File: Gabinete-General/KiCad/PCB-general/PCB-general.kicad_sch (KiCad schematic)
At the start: 6 parts, among them J2 TFT Display, U1 ESP32-S3-DevKitC, U2 LM7805_TO220

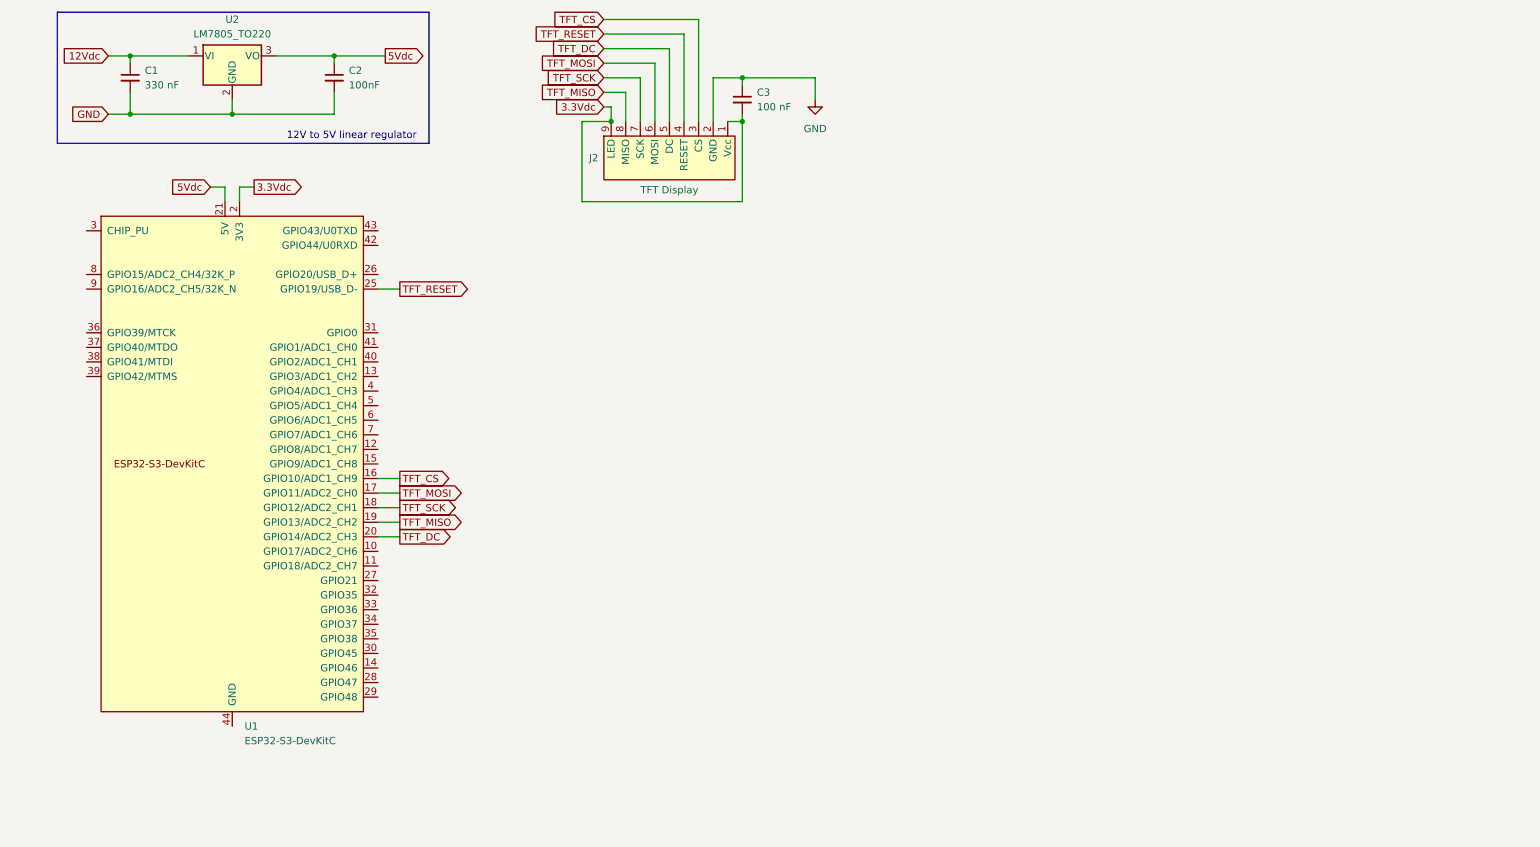
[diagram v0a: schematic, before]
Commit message: Finalizar esquemático PCB control general
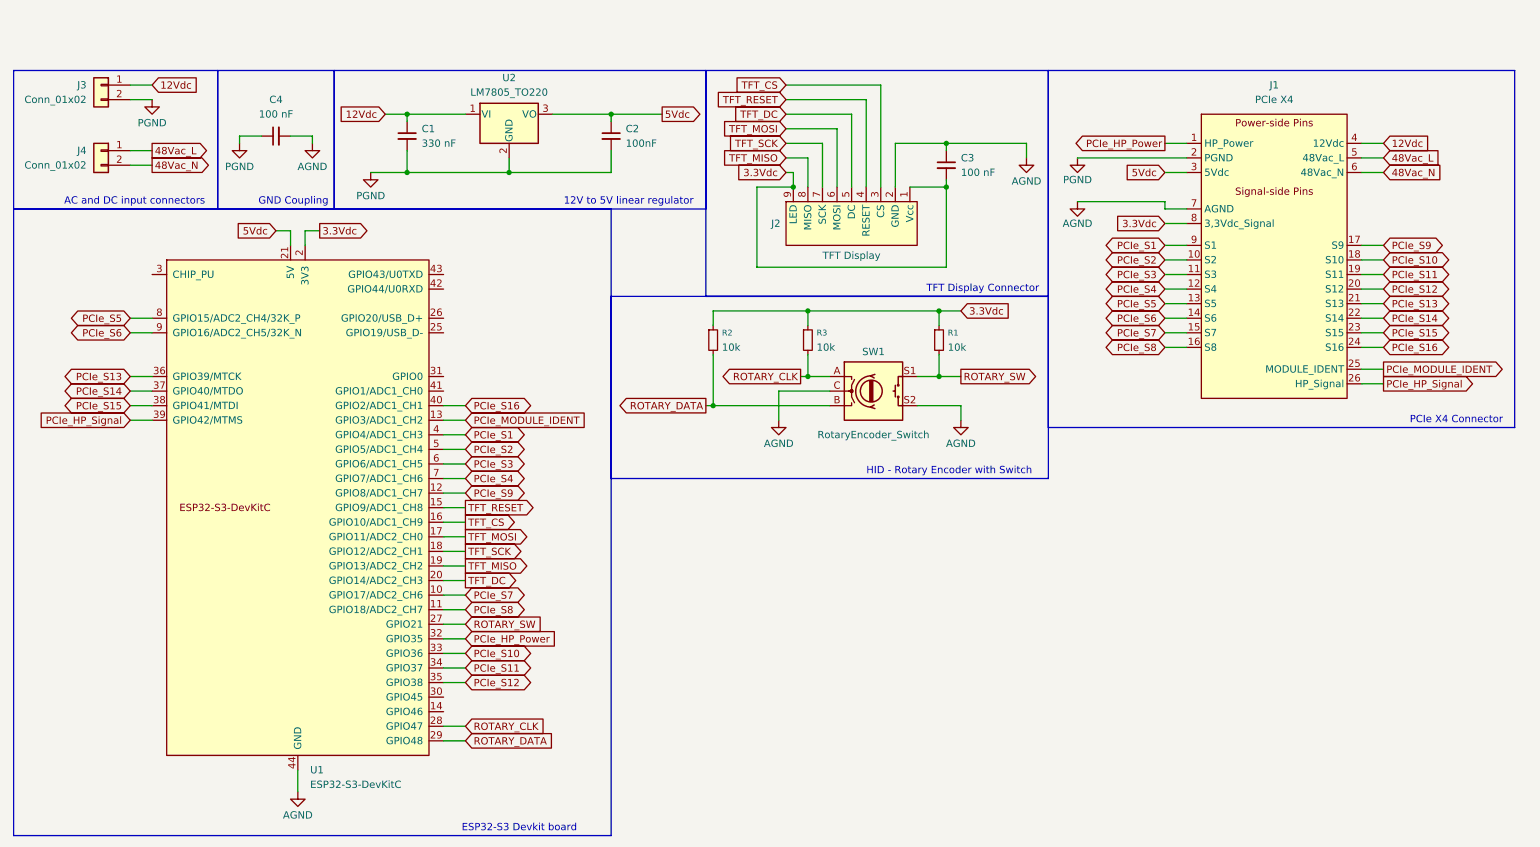
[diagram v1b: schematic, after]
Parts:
- added C4: 100 nF, symbol Device:C_Small
- added J1: PCIe X4, symbol Proyecto_Final:PCIE_x4_NSH_pcb_general
- added J3, J4: Conn_01x02, symbol Connector_Generic:Conn_01x02
- added R1, R2, R3: 10k, symbol Device:R_Small
- added SW1: RotaryEncoder_Switch, symbol Device:RotaryEncoder_Switch
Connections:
- net 12Vdc: now also J1.4 (12Vdc), J3.1 (Pin_1)
- net 3.3Vdc: now also J1.8 (3,3Vdc_Signal), R1.1, R2.1, R3.1
- net 5Vdc: now also J1.3 (5Vdc)
- net TFT_RESET: now also U1.15 (GPIO9/ADC1_CH8); no longer U1.25 (GPIO19/USB_D-)
- net PCIe_S7: now reaches U1.10 (GPIO17/ADC2_CH6)
- net PCIe_S7: now also J1.15 (S7)
- net PCIe_S8: now reaches U1.11 (GPIO18/ADC2_CH7)
- net PCIe_S8: now also J1.16 (S8)
- net PCIe_S9: now reaches U1.12 (GPIO8/ADC1_CH7)
- net PCIe_S9: now also J1.17 (S9)
- net PCIe_MODULE_IDENT: now reaches U1.13 (GPIO3/ADC1_CH2)
- net PCIe_MODULE_IDENT: now also J1.25 (MODULE_IDENT)
- net AGND: now reaches U1.22 (GND), U1.23 (GND), U1.24 (GND), U1.44 (GND)
- net AGND: now also C3.1, J2.2 (GND), C4.2, J1.7 (AGND), SW1.C, SW1.S2
- net ROTARY_SW: now reaches U1.27 (GPIO21)
- net ROTARY_SW: now also R1.2, SW1.S1
- net ROTARY_CLK: now reaches U1.28 (GPIO47)
- net ROTARY_CLK: now also R3.2, SW1.A
- net ROTARY_DATA: now reaches U1.29 (GPIO48)
- net ROTARY_DATA: now also R2.2, SW1.B
- net PCIe_HP_Power: now reaches U1.32 (GPIO35)
- net PCIe_HP_Power: now also J1.1 (HP_Power)
- net PCIe_S10: now reaches U1.33 (GPIO36)
- net PCIe_S10: now also J1.18 (S10)
- net PCIe_S11: now reaches U1.34 (GPIO37)
- net PCIe_S11: now also J1.19 (S11)
- net PCIe_S12: now reaches U1.35 (GPIO38)
- net PCIe_S12: now also J1.20 (S12)
- net PCIe_S13: now reaches U1.36 (GPIO39/MTCK)
- net PCIe_S13: now also J1.21 (S13)
- net PCIe_S14: now reaches U1.37 (GPIO40/MTDO)
- net PCIe_S14: now also J1.22 (S14)
- net PCIe_S15: now reaches U1.38 (GPIO41/MTDI)
- net PCIe_S15: now also J1.23 (S15)
- net PCIe_HP_Signal: now reaches U1.39 (GPIO42/MTMS)
- net PCIe_HP_Signal: now also J1.26 (HP_Signal)
- net PCIe_S1: now reaches U1.4 (GPIO4/ADC1_CH3)
- net PCIe_S1: now also J1.9 (S1)
- net PCIe_S16: now reaches U1.40 (GPIO2/ADC1_CH1)
- net PCIe_S16: now also J1.24 (S16)
- net PCIe_S2: now reaches U1.5 (GPIO5/ADC1_CH4)
- net PCIe_S2: now also J1.10 (S2)
- net PCIe_S3: now reaches U1.6 (GPIO6/ADC1_CH5)
- net PCIe_S3: now also J1.11 (S3)
- net PCIe_S4: now reaches U1.7 (GPIO7/ADC1_CH6)
- net PCIe_S4: now also J1.12 (S4)
- net PCIe_S5: now reaches U1.8 (GPIO15/ADC2_CH4/32K_P)
- net PCIe_S5: now also J1.13 (S5)
- net PCIe_S6: now reaches U1.9 (GPIO16/ADC2_CH5/32K_N)
- net PCIe_S6: now also J1.14 (S6)
- net GND renamed PGND
- net PGND: now also C4.1, J1.2 (PGND), J3.2 (Pin_2); no longer C3.1, J2.2 (GND)
- new net 48Vac_L: J1.5 (48Vac_L), J4.1 (Pin_1)
- new net 48Vac_N: J1.6 (48Vac_N), J4.2 (Pin_2)
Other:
- note added: "AC and DC input connectors"
- note added: "ESP32-S3 Devkit board"
- note added: "GND Coupling"
- note added: "HID - Rotary Encoder with Switch"
- note added: "PCIe X4 Connector"
- note added: "TFT Display Connector"
- title: (none) -> Gabinete general control board
- moved on the sheet: C1, C2, C3, J2, U1, U2

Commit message: Agregar, crear y asignar footprints
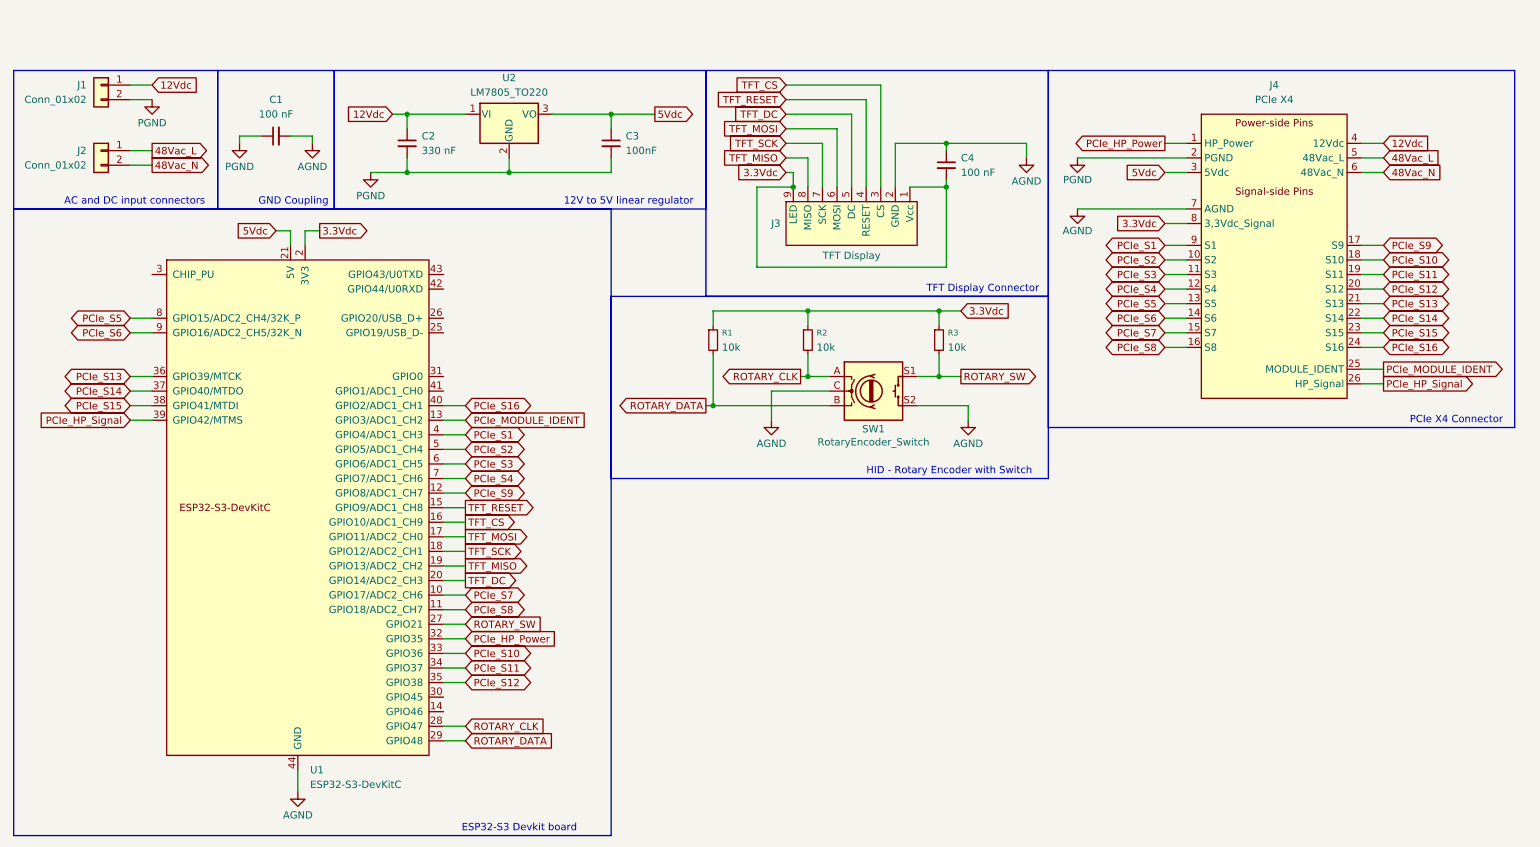
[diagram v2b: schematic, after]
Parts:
- C1: renamed from C4; footprint (none) -> Capacitor_THT:C_Disc_D3.0mm_W2.0mm_P2.50mm
- C2: renamed from C1; footprint (none) -> Capacitor_THT:C_Disc_D3.0mm_W2.0mm_P2.50mm
- C3: renamed from C2; footprint (none) -> Capacitor_THT:C_Disc_D3.0mm_W2.0mm_P2.50mm
- C4: renamed from C3; footprint (none) -> Capacitor_THT:C_Disc_D3.0mm_W2.0mm_P2.50mm
- J1: renamed from J3; footprint (none) -> TerminalBlock_Phoenix:TerminalBlock_Phoenix_MKDS-1,5-2-5.08_1x02_P5.08mm_Horizontal
- J2: renamed from J4; footprint (none) -> TerminalBlock_Phoenix:TerminalBlock_Phoenix_MKDS-1,5-2-5.08_1x02_P5.08mm_Horizontal
- J3: renamed from J2; footprint (none) -> Connector_PinHeader_2.54mm:PinHeader_1x09_P2.54mm_Vertical
- J4: renamed from J1; footprint (none) -> Proyecto_Final:PCIE_x4_Gabinete_NSH
- R1: renamed from R2; footprint (none) -> Resistor_THT:R_Axial_DIN0204_L3.6mm_D1.6mm_P5.08mm_Horizontal
- R2: renamed from R3; footprint (none) -> Resistor_THT:R_Axial_DIN0204_L3.6mm_D1.6mm_P5.08mm_Horizontal
- R3: renamed from R1; footprint (none) -> Resistor_THT:R_Axial_DIN0204_L3.6mm_D1.6mm_P5.08mm_Horizontal
- SW1: footprint (none) -> Rotary_Encoder:RotaryEncoder_Alps_EC11E-Switch_Vertical_H20mm
- U1: footprint PCM_Espressif:ESP32-S3-DevKitC -> Espressif:ESP32-S3-DevKitC_NSH
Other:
- moved on the sheet: C2, C3

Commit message: Diseño inicial PCB
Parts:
- SW1: footprint Rotary_Encoder:RotaryEncoder_Alps_EC11E-Switch_Vertical_H20mm -> Connector_PinHeader_2.54mm:PinHeader_1x05_P2.54mm_Vertical
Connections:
- net TFT_CS: now also U1.20 (GPIO14/ADC2_CH3); no longer U1.16 (GPIO10/ADC1_CH9)
- net TFT_DC: now also U1.18 (GPIO12/ADC2_CH1); no longer U1.20 (GPIO14/ADC2_CH3)
- net TFT_MISO: now also U1.15 (GPIO9/ADC1_CH8); no longer U1.19 (GPIO13/ADC2_CH2)
- net TFT_RESET: now also U1.19 (GPIO13/ADC2_CH2); no longer U1.15 (GPIO9/ADC1_CH8)
- net TFT_SCK: now also U1.16 (GPIO10/ADC1_CH9); no longer U1.18 (GPIO12/ADC2_CH1)
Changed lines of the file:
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@@
 	(wire
 		(pts
+			(xy 96.52 119.38) (xy 92.71 119.38)
+		)
+		(stroke
+			(width 0)
+			(type default)
+		)
+	)
+	(wire
+		(pts
 			(xy 96.52 147.32) (xy 92.71 147.32)
 		)
@@
 	(wire
 		(pts
-			(xy 92.71 114.3) (xy 96.52 114.3)
-		)
-		(stroke
-			(width 0)
-			(type default)
-		)
-	)
-	(wire
-		(pts
 			(xy 92.71 104.14) (xy 96.52 104.14)
 		)
@@
 	(wire
 		(pts
-			(xy 139.7 82.55) (xy 139.7 91.44)
+			(xy 96.52 109.22) (xy 92.71 109.22)
 		)
 		(stroke
@@
 	(wire
 		(pts
-			(xy 92.71 111.76) (xy 96.52 111.76)
+			(xy 139.7 82.55) (xy 139.7 91.44)
 		)
 		(stroke
@@
 	(wire
 		(pts
-			(xy 92.71 109.22) (xy 96.52 109.22)
-		)
-		(stroke
-			(width 0)
-			(type default)
-		)
-	)
-	(wire
-		(pts
-			(xy 92.71 119.38) (xy 96.52 119.38)
-		)
-		(stroke
-			(width 0)
-			(type default)
-		)
-	)
-	(wire
-		(pts
 			(xy 96.52 149.86) (xy 92.71 149.86)
 		)
@@
 	(wire
 		(pts
+			(xy 96.52 121.92) (xy 92.71 121.92)
+		)
+		(stroke
+			(width 0)
+			(type default)
+		)
+	)
+	(wire
+		(pts
 			(xy 138.43 91.44) (xy 139.7 91.44)
 		)
@@
 	(wire
 		(pts
-			(xy 92.71 121.92) (xy 96.52 121.92)
-		)
-		(stroke
-			(width 0)
-			(type default)
-		)
-	)
-	(wire
-		(pts
 			(xy 179.07 86.36) (xy 182.88 86.36)
 		)
@@
 	(wire
 		(pts
-			(xy 92.71 116.84) (xy 96.52 116.84)
+			(xy 218.44 63.5) (xy 222.25 63.5)
 		)
 		(stroke
@@
 	(wire
 		(pts
-			(xy 218.44 63.5) (xy 222.25 63.5)
+			(xy 156.21 74.93) (xy 179.07 74.93)
 		)
 		(stroke
@@
 	(wire
 		(pts
-			(xy 156.21 74.93) (xy 179.07 74.93)
+			(xy 252.73 63.5) (xy 256.54 63.5)
 		)
 		(stroke
@@
 	(wire
 		(pts
-			(xy 252.73 63.5) (xy 256.54 63.5)
+			(xy 252.73 68.58) (xy 256.54 68.58)
 		)
 		(stroke
@@
 	(wire
 		(pts
-			(xy 252.73 68.58) (xy 256.54 68.58)
+			(xy 180.34 45.72) (xy 180.34 46.99)
 		)
 		(stroke
@@
 	(wire
 		(pts
-			(xy 180.34 45.72) (xy 180.34 46.99)
+			(xy 180.34 53.34) (xy 180.34 67.31)
 		)
 		(stroke
@@
 	(wire
 		(pts
-			(xy 180.34 53.34) (xy 180.34 67.31)
+			(xy 69.85 44.45) (xy 69.85 45.72)
 		)
 		(stroke
@@
 	(wire
 		(pts
-			(xy 69.85 44.45) (xy 69.85 45.72)
+			(xy 96.52 111.76) (xy 92.71 111.76)
 		)
 		(stroke
@@
 	(wire
 		(pts
+			(xy 96.52 114.3) (xy 92.71 114.3)
+		)
+		(stroke
+			(width 0)
+			(type default)
+		)
+	)
+	(wire
+		(pts
 			(xy 92.71 139.7) (xy 96.52 139.7)
 		)
@@
 	(wire
 		(pts
+			(xy 96.52 116.84) (xy 92.71 116.84)
+		)
+		(stroke
+			(width 0)
+			(type default)
+		)
+	)
+	(wire
+		(pts
 			(xy 194.31 45.72) (xy 180.34 45.72)
 		)
@@
 	(global_label "TFT_MISO"
 		(shape output)
-		(at 96.52 119.38 0)
+		(at 96.52 109.22 0)
 		(fields_autoplaced yes)
 		(effects
@@
 		)
 		(property "Intersheetrefs" "${INTERSHEET_REFS}"
-			(at 108.0928 119.38 0)
+			(at 108.0928 109.22 0)
 			(effects
 				(font
@@
 	(global_label "TFT_RESET"
 		(shape output)
-		(at 96.52 109.22 0)
+		(at 96.52 119.38 0)
 		(fields_autoplaced yes)
 		(effects
@@
 		)
 		(property "Intersheetrefs" "${INTERSHEET_REFS}"
-			(at 109.2417 109.22 0)
+			(at 109.2417 119.38 0)
 			(effects
 				(font
@@
 	(global_label "TFT_DC"
 		(shape output)
-		(at 96.52 121.92 0)
+		(at 96.52 116.84 0)
 		(fields_autoplaced yes)
 		(effects
@@
 		)
 		(property "Intersheetrefs" "${INTERSHEET_REFS}"
-			(at 106.0366 121.92 0)
+			(at 106.0366 116.84 0)
 			(effects
 				(font
@@
 	(global_label "TFT_CS"
 		(shape output)
-		(at 96.52 111.76 0)
+		(at 96.52 121.92 0)
 		(fields_autoplaced yes)
 		(effects
@@
 		)
 		(property "Intersheetrefs" "${INTERSHEET_REFS}"
-			(at 105.9761 111.76 0)
+			(at 105.9761 121.92 0)
 			(effects
 				(font
@@
 	(global_label "TFT_SCK"
 		(shape output)
-		(at 96.52 116.84 0)
+		(at 96.52 111.76 0)
 		(fields_autoplaced yes)
 		(effects
@@
 		)
 		(property "Intersheetrefs" "${INTERSHEET_REFS}"
-			(at 107.2461 116.84 0)
+			(at 107.2461 111.76 0)
 			(effects
 				(font
@@
 			)
 		)
-		(property "Footprint" "Rotary_Encoder:RotaryEncoder_Alps_EC11E-Switch_Vertical_H20mm"
+		(property "Footprint" "Connector_PinHeader_2.54mm:PinHeader_1x05_P2.54mm_Vertical"
 			(at 163.83 84.836 0)
 			(effects

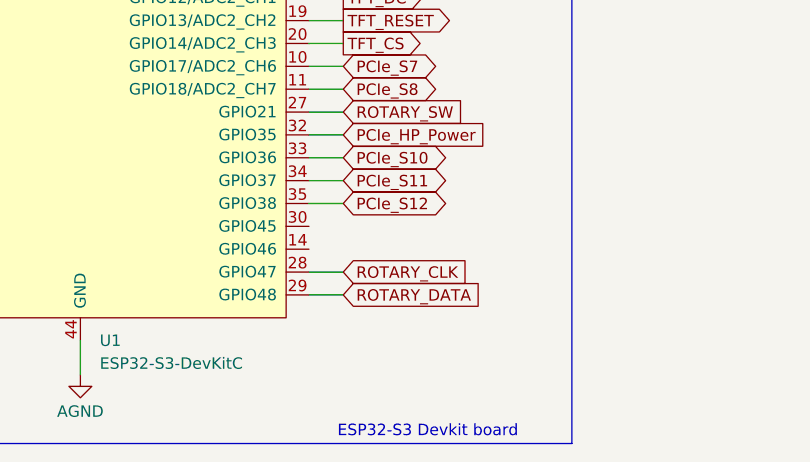
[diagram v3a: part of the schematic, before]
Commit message: Finalizar diseño PCB apta para planchado
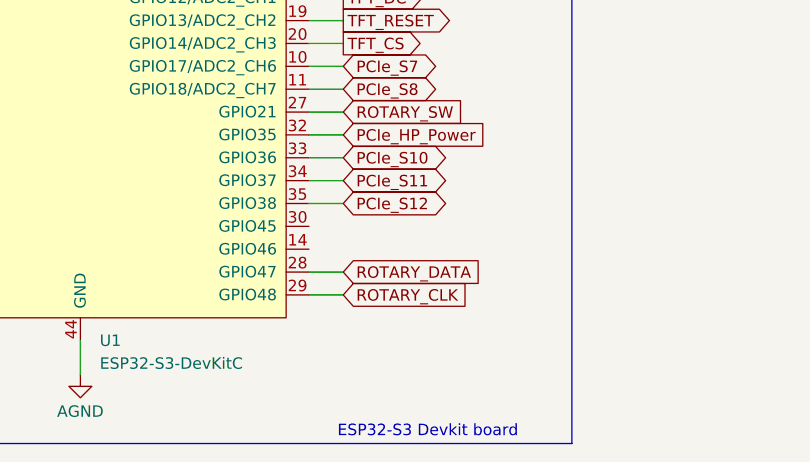
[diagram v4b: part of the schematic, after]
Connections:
- net ROTARY_CLK: now also U1.29 (GPIO48); no longer U1.28 (GPIO47)
- net ROTARY_DATA: now also U1.28 (GPIO47); no longer U1.29 (GPIO48)
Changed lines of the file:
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@@
-	(wire
-		(pts
-			(xy 96.52 147.32) (xy 92.71 147.32)
-		)
-		(stroke
-			(width 0)
-			(type default)
-		)
-	)
 	(wire
 		(pts
@@
 	(wire
 		(pts
-			(xy 96.52 149.86) (xy 92.71 149.86)
-		)
-		(stroke
-			(width 0)
-			(type default)
-		)
-	)
-	(wire
-		(pts
 			(xy 171.45 53.34) (xy 171.45 45.72)
 		)
@@
 	(wire
 		(pts
+			(xy 92.71 147.32) (xy 96.52 147.32)
+		)
+		(stroke
+			(width 0)
+			(type default)
+		)
+	)
+	(wire
+		(pts
 			(xy 92.71 93.98) (xy 96.52 93.98)
 		)
@@
 		(pts
 			(xy 66.04 63.5) (xy 66.04 60.96)
+		)
+		(stroke
+			(width 0)
+			(type default)
+		)
+	)
+	(wire
+		(pts
+			(xy 92.71 149.86) (xy 96.52 149.86)
 		)
 		(stroke
@@
 	(global_label "ROTARY_CLK"
 		(shape input)
-		(at 96.52 147.32 0)
-		(fields_autoplaced yes)
-		(effects
-			(font
-				(size 1.27 1.27)
-			)
-			(justify left)
-		)
-		(property "Intersheetrefs" "${INTERSHEET_REFS}"
-			(at 111.0562 147.32 0)
+		(at 96.52 149.86 0)
+		(fields_autoplaced yes)
+		(effects
+			(font
+				(size 1.27 1.27)
+			)
+			(justify left)
+		)
+		(property "Intersheetrefs" "${INTERSHEET_REFS}"
+			(at 111.0562 149.86 0)
 			(effects
 				(font
@@
 	(global_label "ROTARY_DATA"
 		(shape input)
-		(at 96.52 149.86 0)
-		(fields_autoplaced yes)
-		(effects
-			(font
-				(size 1.27 1.27)
-			)
-			(justify left)
-		)
-		(property "Intersheetrefs" "${INTERSHEET_REFS}"
-			(at 111.9029 149.86 0)
-			(effects
-				(font
+		(at 96.52 147.32 0)
+		(fields_autoplaced yes)
+		(effects
+			(font
+				(size 1.27 1.27)
+			)
+			(justify left)
+		)
+		(property "Intersheetrefs" "${INTERSHEET_REFS}"
+			(at 111.9029 147.32 0)
+			(effects
+				(font
